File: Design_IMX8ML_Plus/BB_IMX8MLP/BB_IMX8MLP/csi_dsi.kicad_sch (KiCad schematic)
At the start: 15 parts, among them J12 DSI, J13 CSI Camera1, J17 CSI Camera2, U21 PCMF3USB3S, U22 PCMF3USB3S, U23 PCMF3USB3S

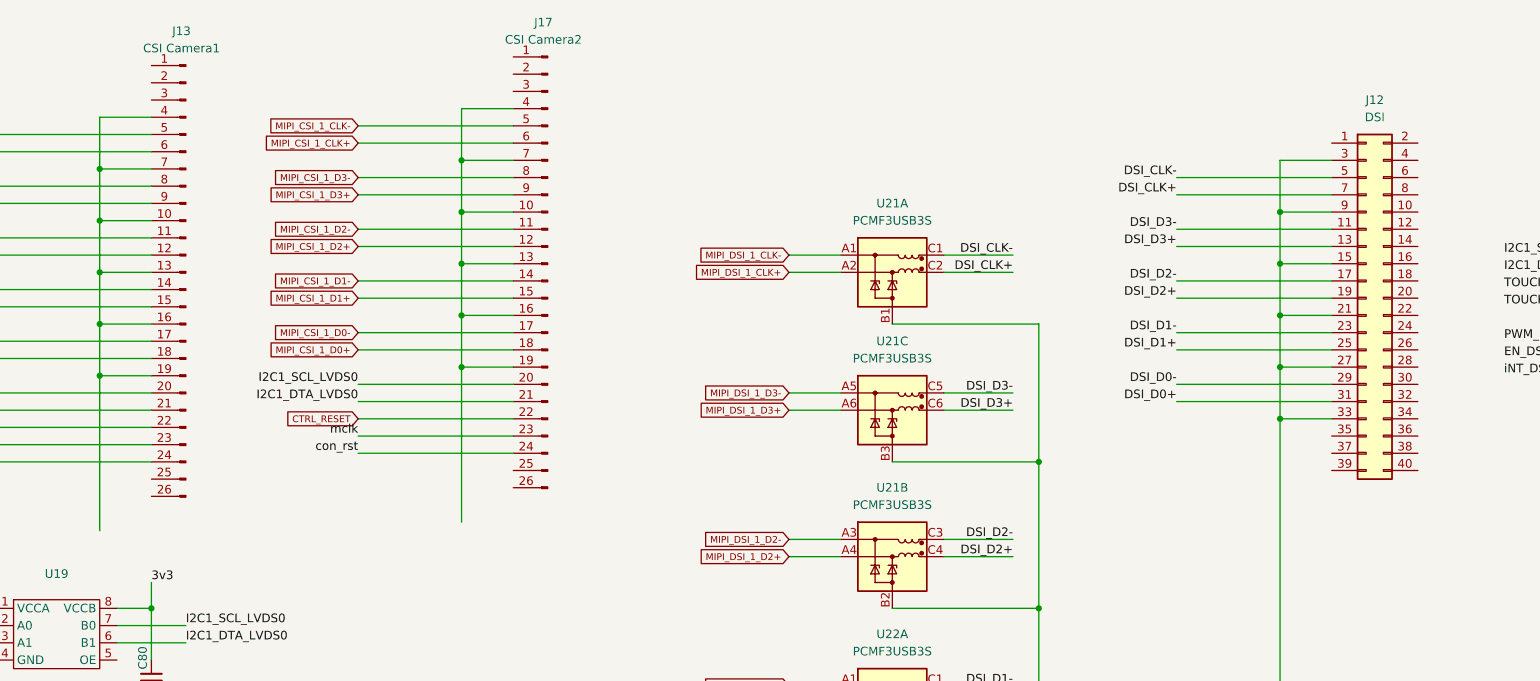
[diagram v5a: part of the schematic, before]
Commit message: reorganization of the componentes
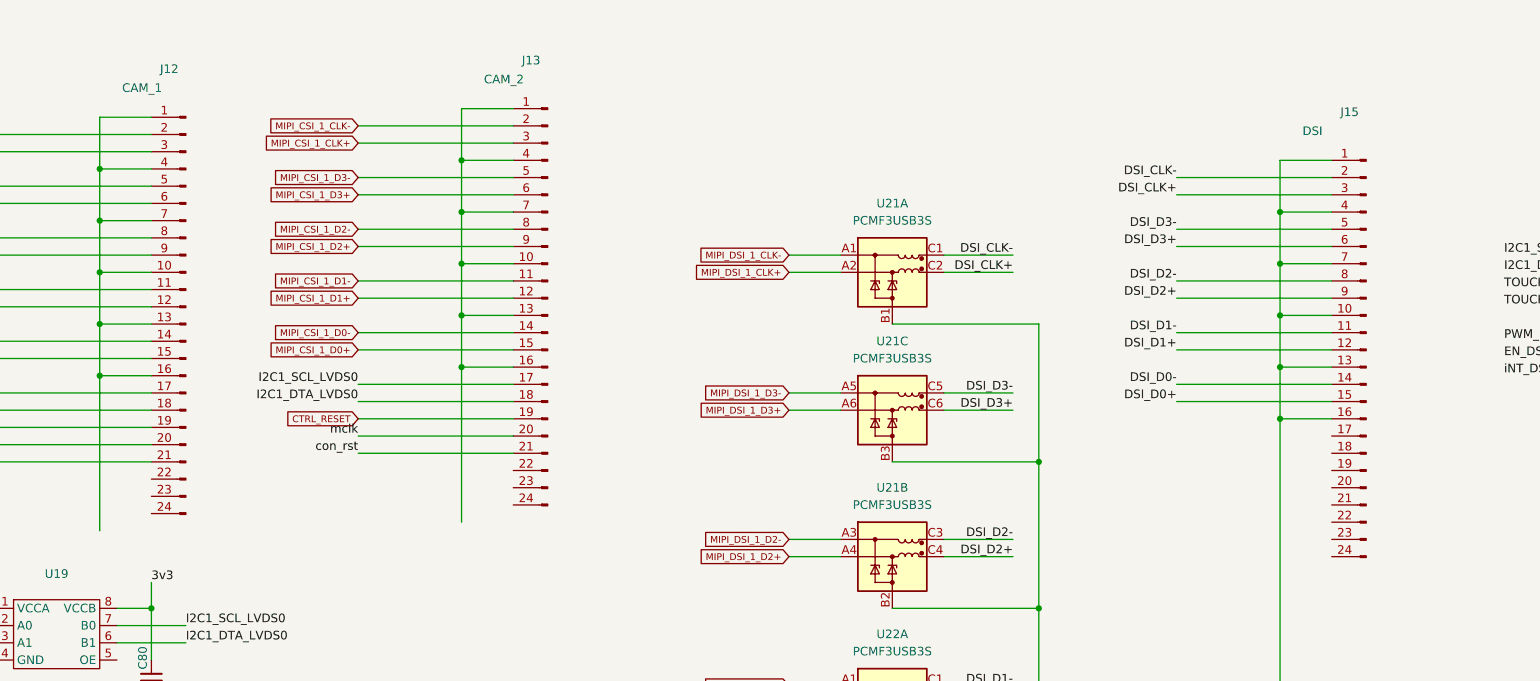
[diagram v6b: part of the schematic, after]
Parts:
- removed J12: DSI, symbol Connector_Generic:Conn_02x20_Odd_Even
- removed J13: CSI Camera1, symbol Connector:Conn_01x26_Pin
- removed J17: CSI Camera2, symbol Connector:Conn_01x26_Pin
- added J12: CAM_1, Connector_FFC-FPC:Hirose_FH12-24S-0.5SH_1x24-1MP_P0.50mm_Horizontal, symbol Connector:Conn_01x24_Pin
- added J13: CAM_2, Connector_FFC-FPC:Hirose_FH12-24S-0.5SH_1x24-1MP_P0.50mm_Horizontal, symbol Connector:Conn_01x24_Pin
- added J15: DSI, Connector_FFC-FPC:Hirose_FH12-24S-0.5SH_1x24-1MP_P0.50mm_Horizontal, symbol Connector:Conn_01x24_Pin
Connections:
- net CTRL_RESET: now also J12.19 (Pin_19), J13.19 (Pin_19)
- net DSI_CLK+: now also J15.3 (Pin_3)
- net DSI_CLK-: now also J15.2 (Pin_2)
- net DSI_D0+: now also J15.15 (Pin_15)
- net DSI_D0-: now also J15.14 (Pin_14)
- net DSI_D1+: now also J15.12 (Pin_12)
- net DSI_D1-: now also J15.11 (Pin_11)
- net DSI_D2+: now also J15.9 (Pin_9)
- net DSI_D2-: now also J15.8 (Pin_8)
- net DSI_D3+: now also J15.6 (Pin_6)
- net DSI_D3-: now also J15.5 (Pin_5)
- net GND: now also J15.1 (Pin_1), J15.10 (Pin_10), J15.13 (Pin_13), J15.16 (Pin_16), J15.4 (Pin_4), J15.7 (Pin_7)
- net I2C1_DTA_LVDS0: now also J12.18 (Pin_18), J13.18 (Pin_18)
- net I2C1_SCL_LVDS0: now also J12.17 (Pin_17), J13.17 (Pin_17)
- net MIPI_CSI_1_CLK+: now also J12.3 (Pin_3), J13.3 (Pin_3)
- net MIPI_CSI_1_CLK-: now also J12.2 (Pin_2), J13.2 (Pin_2)
- net MIPI_CSI_1_D0+: now also J12.15 (Pin_15), J13.15 (Pin_15)
- net MIPI_CSI_1_D0-: now also J12.14 (Pin_14), J13.14 (Pin_14)
- net MIPI_CSI_1_D1+: now also J12.12 (Pin_12), J13.12 (Pin_12)
- net MIPI_CSI_1_D1-: now also J12.11 (Pin_11), J13.11 (Pin_11)
- net MIPI_CSI_1_D2+: now also J12.9 (Pin_9), J13.9 (Pin_9)
- net MIPI_CSI_1_D2-: now also J12.8 (Pin_8), J13.8 (Pin_8)
- net MIPI_CSI_1_D3+: now also J12.6 (Pin_6), J13.6 (Pin_6)
- net MIPI_CSI_1_D3-: now also J12.5 (Pin_5), J13.5 (Pin_5)
- net con_rst: now also J12.21 (Pin_21), J13.21 (Pin_21)
- net mclk: now also J12.20 (Pin_20), J13.20 (Pin_20)
- new net: J12.1 (Pin_1), J12.10 (Pin_10), J12.13 (Pin_13), J12.16 (Pin_16), J12.4 (Pin_4), J12.7 (Pin_7)
- new net: J13.1 (Pin_1), J13.10 (Pin_10), J13.13 (Pin_13), J13.16 (Pin_16), J13.4 (Pin_4), J13.7 (Pin_7)

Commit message: Board base resize
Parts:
- removed U21, U22, U23: PCMF3USB3S, Package_CSP:Nexperia_WLCSP-15_6-3-6_2.37x1.17mm_Layout6x3_P0.4mm, symbol Power_Protection:PCMF3USB3S
- added L10, L11, L12, L13, L14, L15, L16, L7, L8, L9: 12R@100MHz, _W_SBC:FIL_EXC-14CH120U, symbol Device:L_Ferrite_Coupled_Small_1324
- added U21, U23, U44, U45, U46, U47, U48: ~, _W_SBC:DFN10_U-DFN2510-10_DIO, symbol _W_MX8M:D3V3F4U10LP-7
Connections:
- net DSI_CLK+ is gone; now on net MIPI_DSI_1_CLK+: J15.3 (Pin_3)
- net DSI_CLK- is gone; now on net MIPI_DSI_1_CLK-: J15.2 (Pin_2)
- net DSI_D0+ is gone; now on net MIPI_DSI_1_D0+: J15.15 (Pin_15)
- net DSI_D0- is gone; now on net MIPI_DSI_1_D0-: J15.14 (Pin_14)
- net DSI_D1+ is gone; now on net MIPI_DSI_1_D1+: J15.12 (Pin_12)
- net DSI_D1- is gone; now on net MIPI_DSI_1_D1-: J15.11 (Pin_11)
- net DSI_D2+ is gone; now on net MIPI_DSI_1_D2+: J15.9 (Pin_9)
- net DSI_D2- is gone; now on net MIPI_DSI_1_D2-: J15.8 (Pin_8)
- net DSI_D3+ is gone; now on net MIPI_DSI_1_D3+: J15.6 (Pin_6)
- net DSI_D3- is gone; now on net MIPI_DSI_1_D3-: J15.5 (Pin_5)
- net GND: now also U21.3 (GND), U21.8 (GND), U23.3 (GND), U23.8 (GND), U44.3 (GND), U44.8 (GND), U45.3 (GND), U45.8 (GND), U46.3 (GND), U46.8 (GND), U47.3 (GND), U47.8 (GND), U48.3 (GND), U48.8 (GND)
- net MIPI_CSI_1_CLK+: now also J12.15 (Pin_15), L7.2, L7.4, U23.2 (I/O); no longer J12.3 (Pin_3), J13.3 (Pin_3)
- net MIPI_CSI_1_CLK-: now also J12.14 (Pin_14), L7.1, L7.3, U23.1 (I/O); no longer J12.2 (Pin_2), J13.2 (Pin_2)
- net MIPI_CSI_1_D0+: now also J12.12 (Pin_12), L11.2, L11.4, U45.2 (I/O); no longer J12.15 (Pin_15), J13.15 (Pin_15)
- net MIPI_CSI_1_D0-: now also J12.11 (Pin_11), L11.1, L11.3, U45.1 (I/O); no longer J12.14 (Pin_14), J13.14 (Pin_14)
- net MIPI_CSI_1_D1+: now also J12.9 (Pin_9), L10.2, L10.4, U44.5 (I/O); no longer J12.12 (Pin_12), J13.12 (Pin_12)
- net MIPI_CSI_1_D1-: now also J12.8 (Pin_8), L10.1, L10.3, U44.4 (I/O); no longer J12.11 (Pin_11), J13.11 (Pin_11)
- net MIPI_CSI_1_D2+: now also J12.6 (Pin_6), L9.2, L9.4, U44.2 (I/O); no longer J12.9 (Pin_9), J13.9 (Pin_9)
- net MIPI_CSI_1_D2-: now also J12.5 (Pin_5), L9.1, L9.3, U44.1 (I/O); no longer J12.8 (Pin_8), J13.8 (Pin_8)
- net MIPI_CSI_1_D3+: now also J12.3 (Pin_3), L8.2, L8.4, U23.5 (I/O); no longer J12.6 (Pin_6), J13.6 (Pin_6)
- net MIPI_CSI_1_D3-: now also J12.2 (Pin_2), L8.1, L8.3, U23.4 (I/O); no longer J12.5 (Pin_5), J13.5 (Pin_5)
- net MIPI_DSI_1_CLK+: now also U28.2 (I/O)
- net MIPI_DSI_1_CLK-: now also U28.1 (I/O)
- net MIPI_DSI_1_D0+: now also U21.2 (I/O)
- net MIPI_DSI_1_D0-: now also U21.1 (I/O)
- net MIPI_DSI_1_D1+: now also U29.5 (I/O)
- net MIPI_DSI_1_D1-: now also U29.4 (I/O)
- net MIPI_DSI_1_D2+: now also U29.2 (I/O)
- net MIPI_DSI_1_D2-: now also U29.1 (I/O)
- net MIPI_DSI_1_D3+: now also U28.5 (I/O)
- net MIPI_DSI_1_D3-: now also U28.4 (I/O)
- new net: U46.10 (nc), U46.6 (nc), U46.7 (nc), U46.9 (nc)
- new net: U45.10 (nc), U45.6 (nc), U45.7 (nc), U45.9 (nc)
- new net: U23.10 (nc), U23.6 (nc), U23.7 (nc), U23.9 (nc)
- new net: U47.10 (nc), U47.6 (nc), U47.7 (nc), U47.9 (nc)
- new net: U48.10 (nc), U48.6 (nc), U48.7 (nc), U48.9 (nc)
- new net: U44.10 (nc), U44.6 (nc), U44.7 (nc), U44.9 (nc)
- new net: U21.10 (nc), U21.6 (nc), U21.7 (nc), U21.9 (nc)
- new net MIPI_CSI_2_CLK+: J13.15 (Pin_15), L14.2, L14.4, U47.2 (I/O)
- new net MIPI_CSI_2_CLK-: J13.14 (Pin_14), L14.1, L14.3, U47.1 (I/O)
- new net MIPI_CSI_2_D0+: J13.12 (Pin_12), L16.2, L16.4, U48.2 (I/O)
- new net MIPI_CSI_2_D0-: J13.11 (Pin_11), L16.1, L16.3, U48.1 (I/O)
- new net MIPI_CSI_2_D1+: J13.9 (Pin_9), L13.2, L13.4, U46.5 (I/O)
- new net MIPI_CSI_2_D1-: J13.8 (Pin_8), L13.1, L13.3, U46.4 (I/O)
- new net MIPI_CSI_2_D2+: J13.6 (Pin_6), L12.2, L12.4, U46.2 (I/O)
- new net MIPI_CSI_2_D2-: J13.5 (Pin_5), L12.1, L12.3, U46.1 (I/O)
- new net MIPI_CSI_2_D3+: J13.3 (Pin_3), L15.2, L15.4, U47.5 (I/O)
- new net MIPI_CSI_2_D3-: J13.2 (Pin_2), L15.1, L15.3, U47.4 (I/O)
- no-connect marks 2 -> 15
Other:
- moved on the sheet: C79, C80, J13, R64, R65, R66, R67, U19, U28, U29

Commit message: pcb reorganization
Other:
- moved on the sheet: C79, C80, R64, R65, R66, R67, U19
